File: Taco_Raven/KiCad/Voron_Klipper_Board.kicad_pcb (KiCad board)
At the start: 4 copper layers, 120 x 113 mm, 360 parts, among them J1 CONN_02X05, J10 CONN_01X04, J11 CONN_01X04, J12 CONN_02X03, J13 CONN_01X02, J14 CONN_01X02, J15 CONN_01X02, J16 CONN_01X02, J17 CONN_01X02, J18 CONN_01X02, J19 CONN_01X02, J2 CONN_02X05, J20 CONN_01X02, J21 CONN_01X02, J22 CONN_01X02, J23 CONN_01X02, J24 CONN_01X02, J25 CONN_01X06, J26 CONN_01X02, J27 CONN_01X02, J28 CONN_01X02, J29 CONN_01X03, J3 CONN_01X04, J30 CONN_01X03, J31 CONN_01X03, J32 CONN_01X03, J33 CONN_01X03, J34 USB_MINI, J35 CONN_02X05, J36 CONN_02X04, J4 CONN_01X04, J5 CONN_01X04, J6 CONN_01X04, J7 CONN_01X04, J8 CONN_01X04, J9 CONN_01X04, SW1 SW_Push, U1 TMC2130, U10 PMV40UN, U11 PMV40UN, U12 PMV40UN, U13 PMV40UN, U14 CSD18532, U15 CSD18532, U16 CSD18532, U17 CSD18532, U18 AP2112-3.3, U19 A4403, U2 TMC2130, U20 A4403, U21 ATSAMD51, U22 SPIFLASH_SOIC8, U23 PMV40UN, U3 TMC2130, U4 TMC2130, U5 TMC2130, U6 TMC2130, U7 TMC2130, U8 TMC2130, U9 PMV40UN

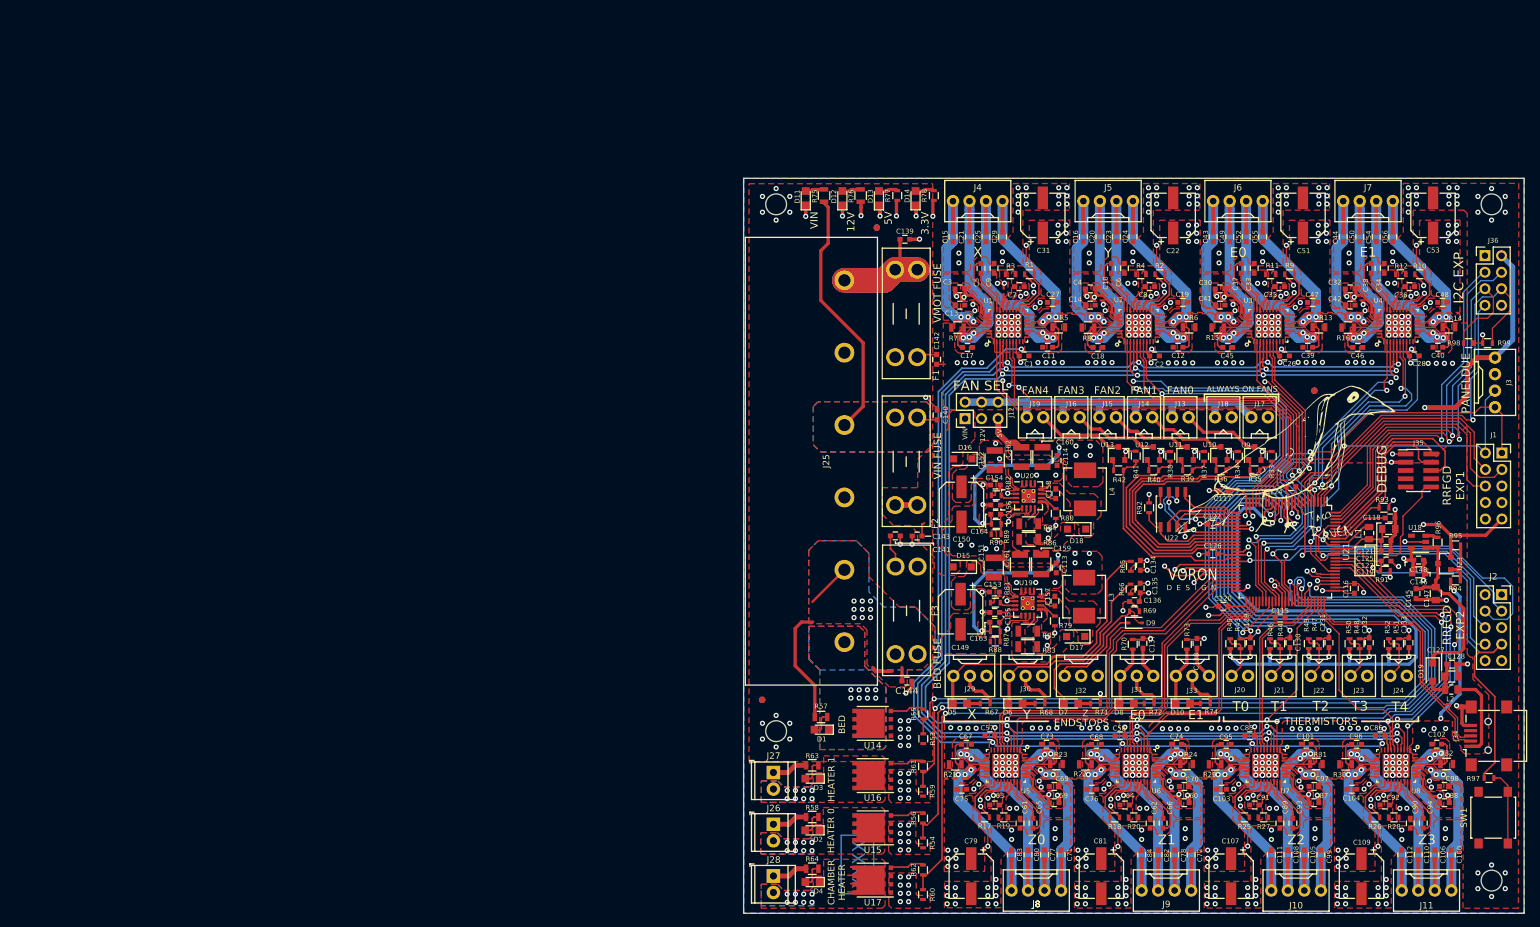
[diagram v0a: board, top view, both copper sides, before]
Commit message: TMC2209 upgrade layout ready for review
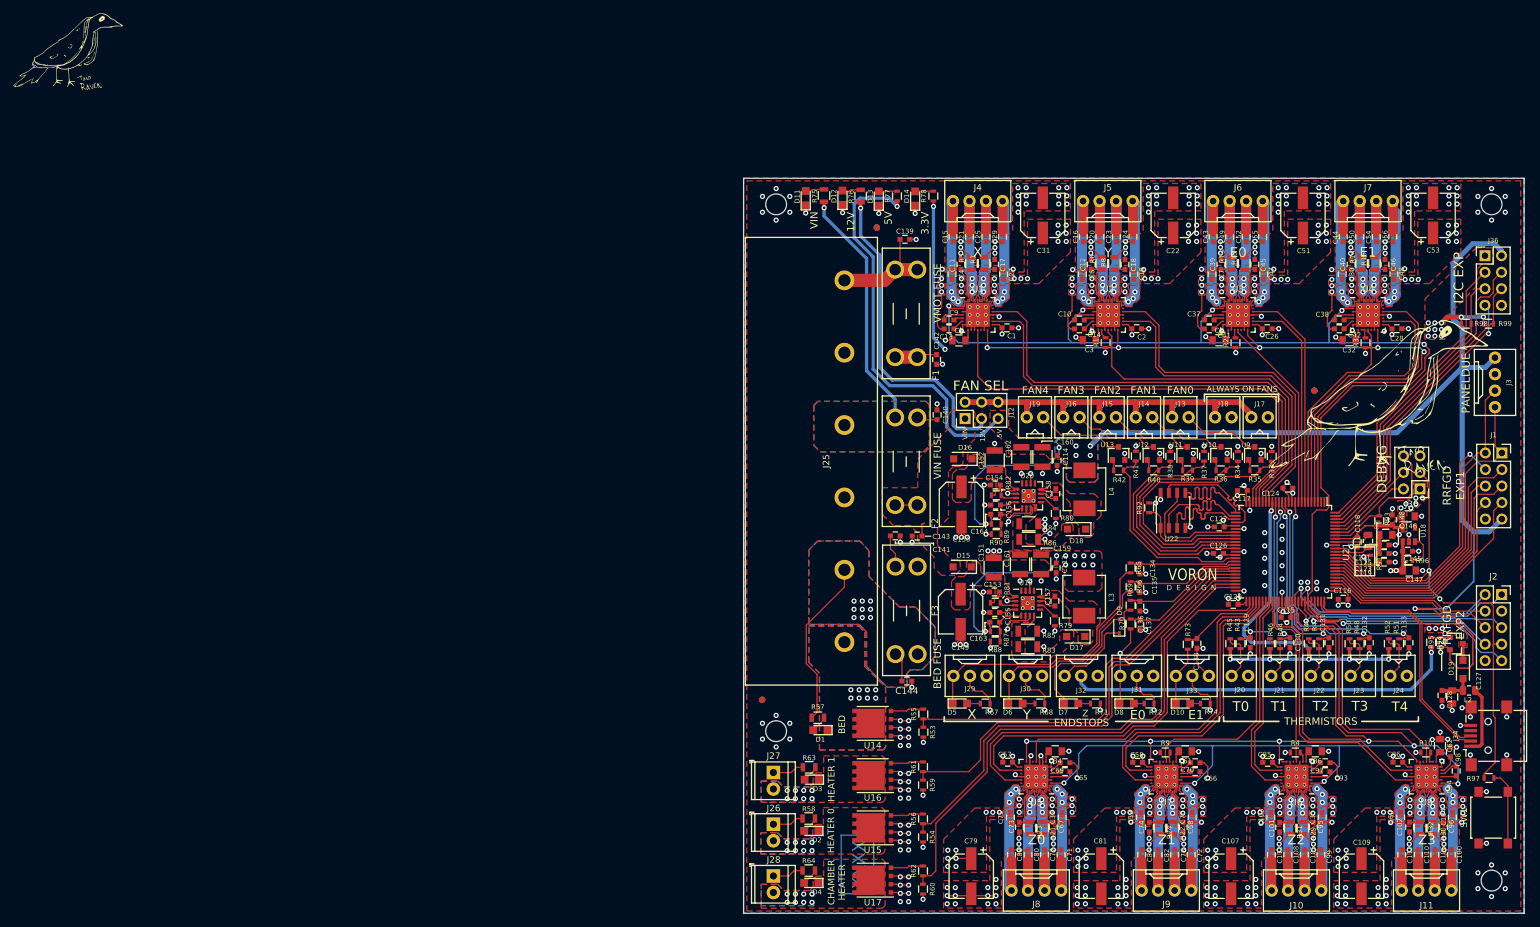
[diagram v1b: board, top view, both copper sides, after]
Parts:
- removed ? (x2): , 
- removed C63, C64, C87, C88, C89, C90, C91, C92: 100nF, MZBOT:C_0603
- removed G***: TACo_Large, MZBOT:TACo_Large
- removed R11, R12, R19, R20, R27, R28: 10R, MZBOT:R_0603
- removed R17, R18, R25, R26: 10.0K, MZBOT:R_0603
- added G1: TACo, MZBOT:taco, F.Cu at (6.78, 20.7)
- C3, C32, C34, C36, C5, C61, C62, C8: value 100nF -> 4.7uF; footprint MZBOT:C_0603 -> MZBOT:C_0805
- J35: value CONN_02X05 -> CONN_02X03; footprint MZBOT:PinHeader_2x05_P1.27mm_Vertical_SMD -> MZBOT:PinHeader_2x03_P2.54mm_Vertical
- R3, R4: value 10R -> 10.0K
- U1, U2, U3, U4, U5, U6, U7, U8: value TMC2130 -> TMC2209; footprint MZBOT:QFN36_0.5_5.0X6.0 -> MZBOT:QFN-28_EP_5x5_Pitch0.5mm
- moved C34 89.8 mm to (157.9, 128.1), turned to 180 degrees
- moved C33 89.4 mm to (159.0, 138.3), turned to 90 degrees
- moved C35 81.9 mm to (199.0, 138.3), turned to 90 degrees
- moved R4 77.3 mm to (194.8, 128.3)
- moved R9 76.0 mm to (174.8, 128.3)
- moved R10 73.5 mm to (214.9, 128.3)
- moved C36 72.9 mm to (197.9, 128.1)
- moved R3 55.6 mm to (205.6, 65.3), turned to 90 degrees
- moved C62 46.1 mm to (217.1, 127.2), turned to 270 degrees
- moved C60 33.3 mm to (211.0, 138.2), turned to 90 degrees
- moved C7 29.7 mm to (182.0, 54.7), turned to 270 degrees
- moved C61 27.7 mm to (177.9, 128.1), turned to 180 degrees
- moved U6 24.7 mm to (195.0, 132.0)
- moved C3 21.4 mm to (163.1, 64.9), turned to 180 degrees
- moved C4 21.4 mm to (142.0, 54.7), turned to 270 degrees
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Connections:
- C100 pad 2: Z3_OA2 -> Z3_OB2
- C105 pad 2: Z2_OA1 -> Z2_OB1
- C106 pad 2: Z3_OA1 -> Z3_OB1
- C108 pad 2: Z2_OB1 -> Z2_OA1
- C110 pad 2: Z3_OB1 -> Z3_OA1
- C111 pad 2: Z2_OB2 -> Z2_OA2
- C112 pad 2: Z3_OB2 -> Z3_OA2
- C129 pad 2: T0 -> T4
- C130 pad 2: T1 -> T3
- C132 pad 2: T3 -> T1
- C133 pad 2: T4 -> T0
- C15 pad 2: X_OA2 -> X_OB2
- C16 pad 2: Y_OA2 -> Y_OB2
- C20 pad 2: Y_OA1 -> Y_OB1
- C21 pad 2: X_OA1 -> X_OB1
- C23 pad 2: Y_OB1 -> Y_OA1
- C24 pad 2: Y_OB2 -> Y_OA2
- C25 pad 2: X_OB1 -> X_OA1
- C29 pad 2: X_OB2 -> X_OA2
- C3 pad 1: GND -> Net-(C3-Pad1)
- C3 pad 2: +5V -> GND
- C30 pad 2: +5V -> VMOT_FUSED
- C32 pad 1: GND -> Net-(C32-Pad1)
- C32 pad 2: +5V -> GND
- C33 pad 2: +5V -> VMOT_FUSED
- C34 pad 2: +5V -> Net-(C34-Pad2)
- C35 pad 2: Net-(C35-Pad2) -> VMOT_FUSED
- C4 pad 2: +5V -> VMOT_FUSED
- C43 pad 2: E0_OA2 -> E0_OB2
- C44 pad 2: E1_OA2 -> E1_OB2
- C49 pad 2: E0_OA1 -> E0_OB1
- C5 pad 2: +5V -> Net-(C5-Pad2)
- C50 pad 2: E1_OA1 -> E1_OB1
- C52 pad 2: E0_OB1 -> E0_OA1
- C54 pad 2: E1_OB1 -> E1_OA1
- C55 pad 2: E0_OB2 -> E0_OA2
- C56 pad 2: E1_OB2 -> E1_OA2
- C59 pad 2: +5V -> VMOT_FUSED
- C6 pad 2: +5V -> VMOT_FUSED
- C60 pad 2: +5V -> VMOT_FUSED
- C61 pad 2: +5V -> Net-(C61-Pad2)
- C62 pad 2: +5V -> Net-(C62-Pad2)
- C7 pad 2: Net-(C7-Pad2) -> VMOT_FUSED
- C71 pad 2: Z0_OA2 -> Z0_OB2
- C72 pad 2: Z1_OA2 -> Z1_OB2
- C77 pad 2: Z0_OA1 -> Z0_OB1
- C78 pad 2: Z1_OA1 -> Z1_OB1
- C80 pad 2: Z0_OB1 -> Z0_OA1
- C82 pad 2: Z1_OB1 -> Z1_OA1
- C83 pad 2: Z0_OB2 -> Z0_OA2
- C84 pad 2: Z1_OB2 -> Z1_OA2
- C99 pad 2: Z2_OA2 -> Z2_OB2
- J1 pad 5: (no net) -> RRFGD_LCD5
- J1 pad 7: (no net) -> RRFGD_LCD7
- J1 pad 8: (no net) -> RRFGD_LCD6
- J10 pad 1: Z2_OB2 -> Z2_OA2
- J10 pad 2: Z2_OB1 -> Z2_OA1
- J10 pad 3: Z2_OA1 -> Z2_OB1
- J10 pad 4: Z2_OA2 -> Z2_OB2
- J11 pad 1: Z3_OB2 -> Z3_OA2
- J11 pad 2: Z3_OB1 -> Z3_OA1
- J11 pad 3: Z3_OA1 -> Z3_OB1
- J11 pad 4: Z3_OA2 -> Z3_OB2
- J2 pad 4: RRFGD_BTN_EN1 -> RRFGD_BTN_EN2
- J2 pad 6: RRFGD_BTN_EN2 -> RRFGD_BTN_EN1
- J2 pad 9: (no net) -> KILL
- J34 pad 4: (no net) -> Net-(J34-Pad4)
- J35 pad 3: GND -> RESETN
- J35 pad 4: SWCLK -> SWO
- J35 pad 5: (no net) -> GND
- J35 pad 6: SWO -> SWCLK
- J4 pad 1: X_OB2 -> X_OA2
- J4 pad 2: X_OB1 -> X_OA1
- J4 pad 3: X_OA1 -> X_OB1
- J4 pad 4: X_OA2 -> X_OB2
- J5 pad 1: Y_OB2 -> Y_OA2
- J5 pad 2: Y_OB1 -> Y_OA1
- J5 pad 3: Y_OA1 -> Y_OB1
- J5 pad 4: Y_OA2 -> Y_OB2
- J6 pad 1: E0_OB2 -> E0_OA2
- J6 pad 2: E0_OB1 -> E0_OA1
- J6 pad 3: E0_OA1 -> E0_OB1
- J6 pad 4: E0_OA2 -> E0_OB2
- J7 pad 1: E1_OB2 -> E1_OA2
- J7 pad 2: E1_OB1 -> E1_OA1
- J7 pad 3: E1_OA1 -> E1_OB1
- J7 pad 4: E1_OA2 -> E1_OB2
- J8 pad 1: Z0_OB2 -> Z0_OA2
- J8 pad 2: Z0_OB1 -> Z0_OA1
- J8 pad 3: Z0_OA1 -> Z0_OB1
- J8 pad 4: Z0_OA2 -> Z0_OB2
- J9 pad 1: Z1_OB2 -> Z1_OA2
- J9 pad 2: Z1_OB1 -> Z1_OA1
- J9 pad 3: Z1_OA1 -> Z1_OB1
- J9 pad 4: Z1_OA2 -> Z1_OB2
- R1 pad 2: DIAG_X -> Net-(R1-Pad2)
- R10 pad 2: DIAG_E1 -> Net-(R10-Pad2)
- R2 pad 2: DIAG_Y -> Net-(R2-Pad2)
- R3 pad 1: +5V -> +3.3V
- R3 pad 2: Net-(C7-Pad2) -> Net-(R3-Pad2)
- R4 pad 1: +5V -> +3.3V
- R4 pad 2: Net-(C8-Pad2) -> Net-(R4-Pad2)
- R43 pad 2: T0 -> T4
- R44 pad 2: T1 -> T3
- R48 pad 2: T3 -> T1
- R51 pad 2: T4 -> T0
- R9 pad 2: DIAG_E0 -> Net-(R9-Pad2)
- U1 pad 1: GND -> X_OB2
- U1 pad 10: (no net) -> GND
- U1 pad 11: GND -> DIAG_X
- U1 pad 12: GND -> Net-(U1-Pad12)
- U1 pad 13: X_OB1 -> GND
- U1 pad 14: Net-(C11-Pad2) -> TMC_UART0
- U1 pad 15: X_OB2 -> +3.3V
- U1 pad 16: VMOT_FUSED -> STEP_X
- U1 pad 17: (no net) -> Net-(U1-Pad17)
- U1 pad 19: (no net) -> DIR_X
- U1 pad 2: SPI_CS_X -> TMC_EN
- U1 pad 20: DIAG_X -> Net-(U1-Pad20)
- U1 pad 21: DIAG_X -> X_OA2
- U1 pad 22: TMC_EN -> VMOT_FUSED
- U1 pad 23: (no net) -> Net-(C17-Pad2)
- U1 pad 24: GND -> X_OA1
- U1 pad 25: Net-(C7-Pad2) -> GND
- U1 pad 26: +5V -> X_OB1
- U1 pad 27: Net-(C9-Pad2) -> Net-(C11-Pad2)
- U1 pad 28: Net-(C9-Pad1) -> VMOT_FUSED
- U1 pad 29: Net-(C13-Pad1) -> GND
- U1 pad 3: SPI_CLK -> GND
- U1 pad 4: SPI_SDI -> Net-(C9-Pad2)
- U1 pad 5: SPI_SDO -> Net-(C9-Pad1)
- U1 pad 6: STEP_X -> Net-(C13-Pad1)
- U1 pad 7: DIR_X -> GND
- U1 pad 8: +3.3V -> Net-(C5-Pad2)
- U1 pad 9: (no net) -> GND
- U18 pad 4: (no net) -> Net-(U18-Pad4)
- U2 pad 1: GND -> Y_OB2
- U2 pad 10: (no net) -> GND
- U2 pad 11: GND -> DIAG_Y
- U2 pad 12: GND -> Net-(U2-Pad12)
- U2 pad 13: Y_OB1 -> GND
- U2 pad 14: Net-(C12-Pad2) -> TMC_UART0
- U2 pad 15: Y_OB2 -> +3.3V
- U2 pad 16: VMOT_FUSED -> STEP_Y
- U2 pad 17: (no net) -> Net-(U2-Pad17)
- U2 pad 19: (no net) -> DIR_Y
- U2 pad 2: SPI_CS_Y -> TMC_EN
- U2 pad 20: DIAG_Y -> Net-(U2-Pad20)
- U2 pad 21: DIAG_Y -> Y_OA2
- U2 pad 22: TMC_EN -> VMOT_FUSED
- U2 pad 23: (no net) -> Net-(C18-Pad2)
- U2 pad 24: GND -> Y_OA1
- U2 pad 25: Net-(C8-Pad2) -> GND
- U2 pad 26: +5V -> Y_OB1
- U2 pad 27: Net-(C10-Pad2) -> Net-(C12-Pad2)
- U2 pad 28: Net-(C10-Pad1) -> VMOT_FUSED
- U2 pad 29: Net-(C14-Pad1) -> GND
- U2 pad 3: SPI_CLK -> GND
- U2 pad 4: SPI_SDI -> Net-(C10-Pad2)
- U2 pad 5: SPI_SDO -> Net-(C10-Pad1)
- U2 pad 6: STEP_Y -> Net-(C14-Pad1)
- U2 pad 7: DIR_Y -> GND
- U2 pad 8: +3.3V -> Net-(C3-Pad1)
- U2 pad 9: (no net) -> Net-(R1-Pad2)
- U21 pad 1: STEP_E1 -> Net-(U21-Pad1)
- U21 pad 100: EXP_I2C_SCL -> EXP_I2C_OSCK
- U21 pad 18: STEP_E0 -> DIR_Y
- U21 pad 2: RRFGD_LCD4 -> Net-(U21-Pad2)
- U21 pad 20: STEP_X -> DIAG_Y
- U21 pad 22: DIAG_X -> STEP_X
- U21 pad 23: SPI_CS_X -> DIAG_X
- U21 pad 3: DIR_E1 -> TMC_UART0
- U21 pad 4: DIAG_E1 -> DIR_E1
- U21 pad 41: RRFGD_SDCSEL -> ENDSTOP_X
- U21 pad 42: SPI_SDI -> ENDSTOP_Y
- U21 pad 43: SPI_CLK -> Z_PROBE
- U21 pad 44: SPI_SDO -> ENDSTOP_E0
- U21 pad 45: DIR_Y -> BED
- U21 pad 46: DIR_Z0 -> HOTEND1
- U21 pad 47: STEP_Z0 -> HOTEND0
- U21 pad 48: DIAG_Z0 -> HEATED_CHAMBER
- U21 pad 49: SPI_CS_Z0 -> DIR_Z0
- U21 pad 5: SPI_CS_E1 -> STEP_E1
- U21 pad 52: DIR_Z1 -> STEP_Z0
- U21 pad 53: STEP_Z1 -> ENDSTOP_E1
- U21 pad 54: DIAG_Z1 -> DIAG_Z0
- U21 pad 55: SPI_CS_Z1 -> DIR_Z1
- U21 pad 56: PD_RX_RRFGD_BUZ -> STEP_Z1
- U21 pad 57: PD_TX_RRFGD_BTN_ENC -> DIAG_Z1
- U21 pad 58: DIAG_Y -> DIR_Z2
- U21 pad 59: SPI_CS_Y -> STEP_Z2
- U21 pad 6: RRFGD_LCDRS -> DIAG_E1
- U21 pad 60: DIR_E0 -> DIAG_Z2
- U21 pad 61: DIAG_E0 -> DIR_Z3
- U21 pad 64: RRFGD_BTN_EN1 -> STEP_Z3
- U21 pad 65: ENDSTOP_X -> TMC_UART1
- U21 pad 66: BED -> SPI_CLK
- U21 pad 67: HOTEND0 -> SPI_SDO
- U21 pad 68: HOTEND1 -> SPI_SDI
- U21 pad 69: HEATED_CHAMBER -> RRFGD_SDDET
- U21 pad 7: RRFGD_LCDE -> DIR_E0
- U21 pad 70: DIR_Z2 -> TMC_EN
- U21 pad 71: STEP_Z2 -> DIAG_Z3
- U21 pad 72: DIAG_Z2 -> KILL
- U21 pad 73: STEP_Z3 -> Net-(U21-Pad73)
- U21 pad 78: ENDSTOP_Y -> RRFGD_BTN_EN1
- U21 pad 79: Z_PROBE -> RRFGD_BTN_EN2
- U21 pad 8: RRFGD_BTN_EN2 -> STEP_E0
- U21 pad 80: ENDSTOP_E0 -> RRFGD_LCD7
- U21 pad 81: ENDSTOP_E1 -> RRFGD_LCD6
- U21 pad 82: SPI_CS_E0 -> RRFGD_LCD5
- U21 pad 83: SPI_CS_Z2 -> RRFGD_LCD4
- U21 pad 84: DIR_Z3 -> RRFGD_LCDRS
- U21 pad 85: DIAG_Z3 -> PD_TX_RRFGD_BTN_ENC
- U21 pad 86: SPI_CS_Z3 -> PD_RX_RRFGD_BUZ
- U21 pad 87: TMC_EN -> RRFGD_LCDE
- U21 pad 9: EXP_I2C_RST -> DIAG_E0
- U21 pad 96: RRFGD_SDDET -> EXP_I2C_RST
- U21 pad 97: EXP_I2C_OSCK -> EXP_I2C_SCL
- U3 pad 1: GND -> E0_OB2
- U3 pad 10: (no net) -> Net-(R2-Pad2)
- U3 pad 11: GND -> DIAG_E0
- U3 pad 12: GND -> Net-(U3-Pad12)
- U3 pad 13: E0_OB1 -> GND
- U3 pad 14: Net-(C39-Pad2) -> TMC_UART0
- U3 pad 15: E0_OB2 -> +3.3V
- U3 pad 16: VMOT_FUSED -> STEP_E0
- U3 pad 17: (no net) -> Net-(U3-Pad17)
- U3 pad 19: (no net) -> DIR_E0
- U3 pad 2: SPI_CS_E0 -> TMC_EN
- U3 pad 20: DIAG_E0 -> Net-(U3-Pad20)
- U3 pad 21: DIAG_E0 -> E0_OA2
- U3 pad 22: TMC_EN -> VMOT_FUSED
- U3 pad 23: (no net) -> Net-(C45-Pad2)
- U3 pad 24: GND -> E0_OA1
- U3 pad 25: Net-(C35-Pad2) -> GND
- U3 pad 26: +5V -> E0_OB1
- U3 pad 27: Net-(C37-Pad2) -> Net-(C39-Pad2)
- U3 pad 28: Net-(C37-Pad1) -> VMOT_FUSED
- U3 pad 29: Net-(C41-Pad1) -> GND
- U3 pad 3: SPI_CLK -> GND
- U3 pad 4: SPI_SDI -> Net-(C37-Pad2)
- U3 pad 5: SPI_SDO -> Net-(C37-Pad1)
- U3 pad 6: STEP_E0 -> Net-(C41-Pad1)
- U3 pad 7: DIR_E0 -> GND
- U3 pad 8: +3.3V -> Net-(C8-Pad2)
- U3 pad 9: (no net) -> GND
- U4 pad 1: GND -> E1_OB2
- U4 pad 10: (no net) -> Net-(R3-Pad2)
- U4 pad 11: GND -> DIAG_E1
- U4 pad 12: GND -> Net-(U4-Pad12)
- U4 pad 13: E1_OB1 -> GND
- U4 pad 14: Net-(C40-Pad2) -> TMC_UART0
- U4 pad 15: E1_OB2 -> +3.3V
- U4 pad 16: VMOT_FUSED -> STEP_E1
- U4 pad 17: (no net) -> Net-(U4-Pad17)
- U4 pad 19: (no net) -> DIR_E1
- U4 pad 2: SPI_CS_E1 -> TMC_EN
- U4 pad 20: DIAG_E1 -> Net-(U4-Pad20)
- U4 pad 21: DIAG_E1 -> E1_OA2
- U4 pad 22: TMC_EN -> VMOT_FUSED
- U4 pad 23: (no net) -> Net-(C46-Pad2)
- U4 pad 24: GND -> E1_OA1
- U4 pad 25: Net-(C36-Pad2) -> GND
- U4 pad 26: +5V -> E1_OB1
- U4 pad 27: Net-(C38-Pad2) -> Net-(C40-Pad2)
- U4 pad 28: Net-(C38-Pad1) -> VMOT_FUSED
- U4 pad 29: Net-(C42-Pad1) -> GND
- U4 pad 3: SPI_CLK -> GND
- U4 pad 4: SPI_SDI -> Net-(C38-Pad2)
- U4 pad 5: SPI_SDO -> Net-(C38-Pad1)
- U4 pad 6: STEP_E1 -> Net-(C42-Pad1)
- U4 pad 7: DIR_E1 -> GND
- U4 pad 8: +3.3V -> Net-(C32-Pad1)
- U4 pad 9: (no net) -> Net-(R3-Pad2)
- U5 pad 1: GND -> Z0_OB2
- U5 pad 10: (no net) -> GND
- U5 pad 11: GND -> DIAG_Z0
- U5 pad 12: GND -> Net-(U5-Pad12)
- U5 pad 13: Z0_OB1 -> GND
- U5 pad 14: Net-(C67-Pad2) -> TMC_UART1
- U5 pad 15: Z0_OB2 -> +3.3V
- U5 pad 16: VMOT_FUSED -> STEP_Z0
- U5 pad 17: (no net) -> Net-(U5-Pad17)
- U5 pad 19: (no net) -> DIR_Z0
- U5 pad 2: SPI_CS_Z0 -> TMC_EN
- U5 pad 20: DIAG_Z0 -> Net-(U5-Pad20)
- U5 pad 21: DIAG_Z0 -> Z0_OA2
- U5 pad 22: TMC_EN -> VMOT_FUSED
- U5 pad 23: (no net) -> Net-(C73-Pad2)
- U5 pad 24: GND -> Z0_OA1
- U5 pad 25: Net-(C63-Pad2) -> GND
- U5 pad 26: +5V -> Z0_OB1
- U5 pad 27: Net-(C65-Pad2) -> Net-(C67-Pad2)
- U5 pad 28: Net-(C65-Pad1) -> VMOT_FUSED
- U5 pad 29: Net-(C69-Pad1) -> GND
- U5 pad 3: SPI_CLK -> GND
- U5 pad 4: SPI_SDI -> Net-(C65-Pad2)
- U5 pad 5: SPI_SDO -> Net-(C65-Pad1)
- U5 pad 6: STEP_Z0 -> Net-(C69-Pad1)
- U5 pad 7: DIR_Z0 -> GND
- U5 pad 8: +3.3V -> Net-(C34-Pad2)
- U5 pad 9: (no net) -> GND
- U6 pad 1: GND -> Z2_OB2
- U6 pad 10: (no net) -> GND
- U6 pad 11: GND -> DIAG_Z2
- U6 pad 12: GND -> Net-(U6-Pad12)
- U6 pad 13: Z1_OB1 -> GND
- U6 pad 14: Net-(C68-Pad2) -> TMC_UART1
- U6 pad 15: Z1_OB2 -> +3.3V
- U6 pad 16: VMOT_FUSED -> STEP_Z2
- U6 pad 17: (no net) -> Net-(U6-Pad17)
- U6 pad 19: (no net) -> DIR_Z2
- U6 pad 2: SPI_CS_Z1 -> TMC_EN
- U6 pad 20: DIAG_Z1 -> Net-(U6-Pad20)
- U6 pad 21: DIAG_Z1 -> Z2_OA2
- U6 pad 22: TMC_EN -> VMOT_FUSED
- U6 pad 23: (no net) -> Net-(C101-Pad2)
- U6 pad 24: GND -> Z2_OA1
- U6 pad 25: Net-(C64-Pad2) -> GND
- U6 pad 26: +5V -> Z2_OB1
- U6 pad 27: Net-(C66-Pad2) -> Net-(C95-Pad2)
- U6 pad 28: Net-(C66-Pad1) -> VMOT_FUSED
- U6 pad 29: Net-(C70-Pad1) -> GND
- U6 pad 3: SPI_CLK -> GND
- U6 pad 4: SPI_SDI -> Net-(C93-Pad2)
- U6 pad 5: SPI_SDO -> Net-(C93-Pad1)
- U6 pad 6: STEP_Z1 -> Net-(C97-Pad1)
- U6 pad 7: DIR_Z1 -> GND
- U6 pad 8: +3.3V -> Net-(C36-Pad2)
- U6 pad 9: (no net) -> Net-(R4-Pad2)
- U7 pad 1: GND -> Z1_OB2
- U7 pad 10: (no net) -> Net-(R9-Pad2)
- U7 pad 11: GND -> DIAG_Z1
- U7 pad 12: GND -> Net-(U7-Pad12)
- U7 pad 13: Z2_OB1 -> GND
- U7 pad 14: Net-(C95-Pad2) -> TMC_UART1
- U7 pad 15: Z2_OB2 -> +3.3V
- U7 pad 16: VMOT_FUSED -> STEP_Z1
- U7 pad 17: (no net) -> Net-(U7-Pad17)
- U7 pad 19: (no net) -> DIR_Z1
- U7 pad 2: SPI_CS_Z2 -> TMC_EN
- U7 pad 20: DIAG_Z2 -> Net-(U7-Pad20)
- U7 pad 21: DIAG_Z2 -> Z1_OA2
- U7 pad 22: TMC_EN -> VMOT_FUSED
- U7 pad 23: (no net) -> Net-(C74-Pad2)
- U7 pad 24: GND -> Z1_OA1
- U7 pad 25: Net-(C91-Pad2) -> GND
- U7 pad 26: +5V -> Z1_OB1
- U7 pad 27: Net-(C93-Pad2) -> Net-(C68-Pad2)
- U7 pad 28: Net-(C93-Pad1) -> VMOT_FUSED
- U7 pad 29: Net-(C97-Pad1) -> GND
- U7 pad 3: SPI_CLK -> GND
- U7 pad 4: SPI_SDI -> Net-(C66-Pad2)
- U7 pad 5: SPI_SDO -> Net-(C66-Pad1)
- U7 pad 6: STEP_Z2 -> Net-(C70-Pad1)
- U7 pad 7: DIR_Z2 -> GND
- U7 pad 8: +3.3V -> Net-(C61-Pad2)
- U7 pad 9: (no net) -> GND
- U8 pad 1: GND -> Z3_OB2
- U8 pad 10: (no net) -> Net-(R10-Pad2)
- U8 pad 11: GND -> DIAG_Z3
- U8 pad 12: GND -> Net-(U8-Pad12)
- U8 pad 13: Z3_OB1 -> GND
- U8 pad 14: Net-(C96-Pad2) -> TMC_UART1
- U8 pad 15: Z3_OB2 -> +3.3V
- U8 pad 16: VMOT_FUSED -> STEP_Z3
- U8 pad 17: (no net) -> Net-(U8-Pad17)
- U8 pad 19: (no net) -> DIR_Z3
- U8 pad 2: SPI_CS_Z3 -> TMC_EN
- U8 pad 20: DIAG_Z3 -> Net-(U8-Pad20)
- U8 pad 21: DIAG_Z3 -> Z3_OA2
- U8 pad 22: TMC_EN -> VMOT_FUSED
- U8 pad 23: (no net) -> Net-(C102-Pad2)
- U8 pad 24: GND -> Z3_OA1
- U8 pad 25: Net-(C92-Pad2) -> GND
- U8 pad 26: +5V -> Z3_OB1
- U8 pad 27: Net-(C94-Pad2) -> Net-(C96-Pad2)
- U8 pad 28: Net-(C94-Pad1) -> VMOT_FUSED
- U8 pad 29: Net-(C98-Pad1) -> GND
- U8 pad 3: SPI_CLK -> GND
- U8 pad 4: SPI_SDI -> Net-(C94-Pad2)
- U8 pad 5: SPI_SDO -> Net-(C94-Pad1)
- U8 pad 6: STEP_Z3 -> Net-(C98-Pad1)
- U8 pad 7: DIR_Z3 -> GND
- U8 pad 8: +3.3V -> Net-(C62-Pad2)
- U8 pad 9: (no net) -> Net-(R10-Pad2)
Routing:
- net +3.3V: track 498.1 -> 127.2 mm, vias 33 -> 48
- net SPI_CLK: track 341.2 -> 37.1 mm, vias 9 -> 1
- net SPI_SDI: track 329.8 -> 33.5 mm, vias 9 -> 1
- net SPI_SDO: track 323.3 -> 35.2 mm, vias 9 -> 1
- net GND: track 170.9 -> 384.8 mm, vias 507 -> 378
- net TMC_UART0: track 0.00 -> 114.1 mm, vias 0 -> 5
- net TMC_UART1: track 0.00 -> 102.6 mm, vias 0 -> 4
- net TMC_EN: track 368.1 -> 282.4 mm, vias 17 -> 10
- net SPI_CS_Y: track 84.6 -> 0.00 mm, vias 2 -> 0
- net SPI_CS_X: track 67.8 -> 0.00 mm
- net HOTEND0: track 134.7 -> 71.6 mm, vias 2 -> 0
- net DIAG_Y: track 114.1 -> 52.7 mm, vias 3 -> 0
- net SPI_CS_Z2: track 61.0 -> 0.00 mm, vias 2 -> 0
- net HOTEND1: track 128.7 -> 67.9 mm, vias 2 -> 0
- net HEATED_CHAMBER: track 140.0 -> 81.4 mm, vias 2 -> 0
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- added copper zone on F.Cu, net +3.3V
- added copper zone on B.Cu, net +5V
- added copper zone on F.Cu, net Net-(C145-Pad2)
- added copper zone on POWER.Cu, net Net-(C145-Pad2)
- removed copper zone on POWER.Cu, net +5V
- removed copper zone on F.Cu, net Net-(C101-Pad2)
- removed copper zone on F.Cu, net Net-(C102-Pad2)
- removed copper zone on F.Cu, net Net-(C11-Pad2)
- removed copper zone on F.Cu, net Net-(C12-Pad2)
- removed copper zone on F.Cu, net Net-(C13-Pad1)
- removed copper zone on F.Cu, net Net-(C14-Pad1)
- removed copper zone on F.Cu, net Net-(C17-Pad2)
- removed copper zone on F.Cu, net Net-(C18-Pad2)
- removed copper zone on F.Cu, net Net-(C35-Pad2)
- removed copper zone on F.Cu, net Net-(C36-Pad2)
- removed copper zone on F.Cu, net Net-(C39-Pad2)
- removed copper zone on F.Cu, net Net-(C40-Pad2)
- removed copper zone on F.Cu, net Net-(C41-Pad1)
- removed copper zone on F.Cu, net Net-(C42-Pad1)
- removed copper zone on F.Cu, net Net-(C45-Pad2)
- removed copper zone on F.Cu, net Net-(C46-Pad2)
- removed copper zone on F.Cu, net Net-(C63-Pad2)
- removed copper zone on F.Cu, net Net-(C64-Pad2)
- removed copper zone on F.Cu, net Net-(C67-Pad2)
- removed copper zone on F.Cu, net Net-(C68-Pad2)
- removed copper zone on F.Cu, net Net-(C69-Pad1)
- removed copper zone on F.Cu, net Net-(C7-Pad2)
- removed copper zone on F.Cu, net Net-(C70-Pad1)
- removed copper zone on F.Cu, net Net-(C73-Pad2)
- removed copper zone on F.Cu, net Net-(C74-Pad2)
- removed copper zone on F.Cu, net Net-(C8-Pad2)
- removed copper zone on F.Cu, net Net-(C91-Pad2)
- removed copper zone on F.Cu, net Net-(C92-Pad2)
- removed copper zone on F.Cu, net Net-(C95-Pad2)
- removed copper zone on F.Cu, net Net-(C96-Pad2)
- removed copper zone on F.Cu, net Net-(C97-Pad1)
- removed copper zone on F.Cu, net Net-(C98-Pad1)
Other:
- net class VREF added: clearance 0.1524, trace_width 0.3048, via_dia 0.8, via_drill 0.4
- rule via_min_drill: 0.3 -> 0.2032
- rule via_min_size: 0.4 -> 0.4572
- board text removed: "U1"
